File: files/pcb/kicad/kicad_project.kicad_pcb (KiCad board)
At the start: 2 copper layers, 100 x 91.5 mm, 107 parts, among them CON1 USB_MINI_B, IC1 ATMEGA328-A, IC10 MY_FET_P, IC11 DS1307, IC12 MY_NPN, IC13 MY_PNP, IC14 MY_FET_N, IC2 74LC138, IC3 TLP627, IC4 TLP627, IC5 SN74141_K155NA, IC6 TLP627-4, IC7 TLP627-4, IC8 MY_3_TERMINAL_REGULATOR, IC9 ICM7555CD, K1 CONN_3, K2 CONN_3, K3 CONN_3, K4 CONN_3, P1 CONN_6, SW3 SW_PUSH, SW4 SW_PUSH, SW5 SW_PUSH, T1 2SC, U1 NEON, U10 NIXIE_IN_16, U11 DC_JACK, U15 MY_PIN52, U16 MY_PIN52, U17 MY_PIN52, U18 MY_PIN52, U2 NEON, U3 NEON, U4 NEON, U5 NIXIE_IN_16, U6 NIXIE_IN_16, U7 NIXIE_IN_16, U8 NIXIE_IN_16, U9 NIXIE_IN_16, X1 12MHz, X2 32.768kHz

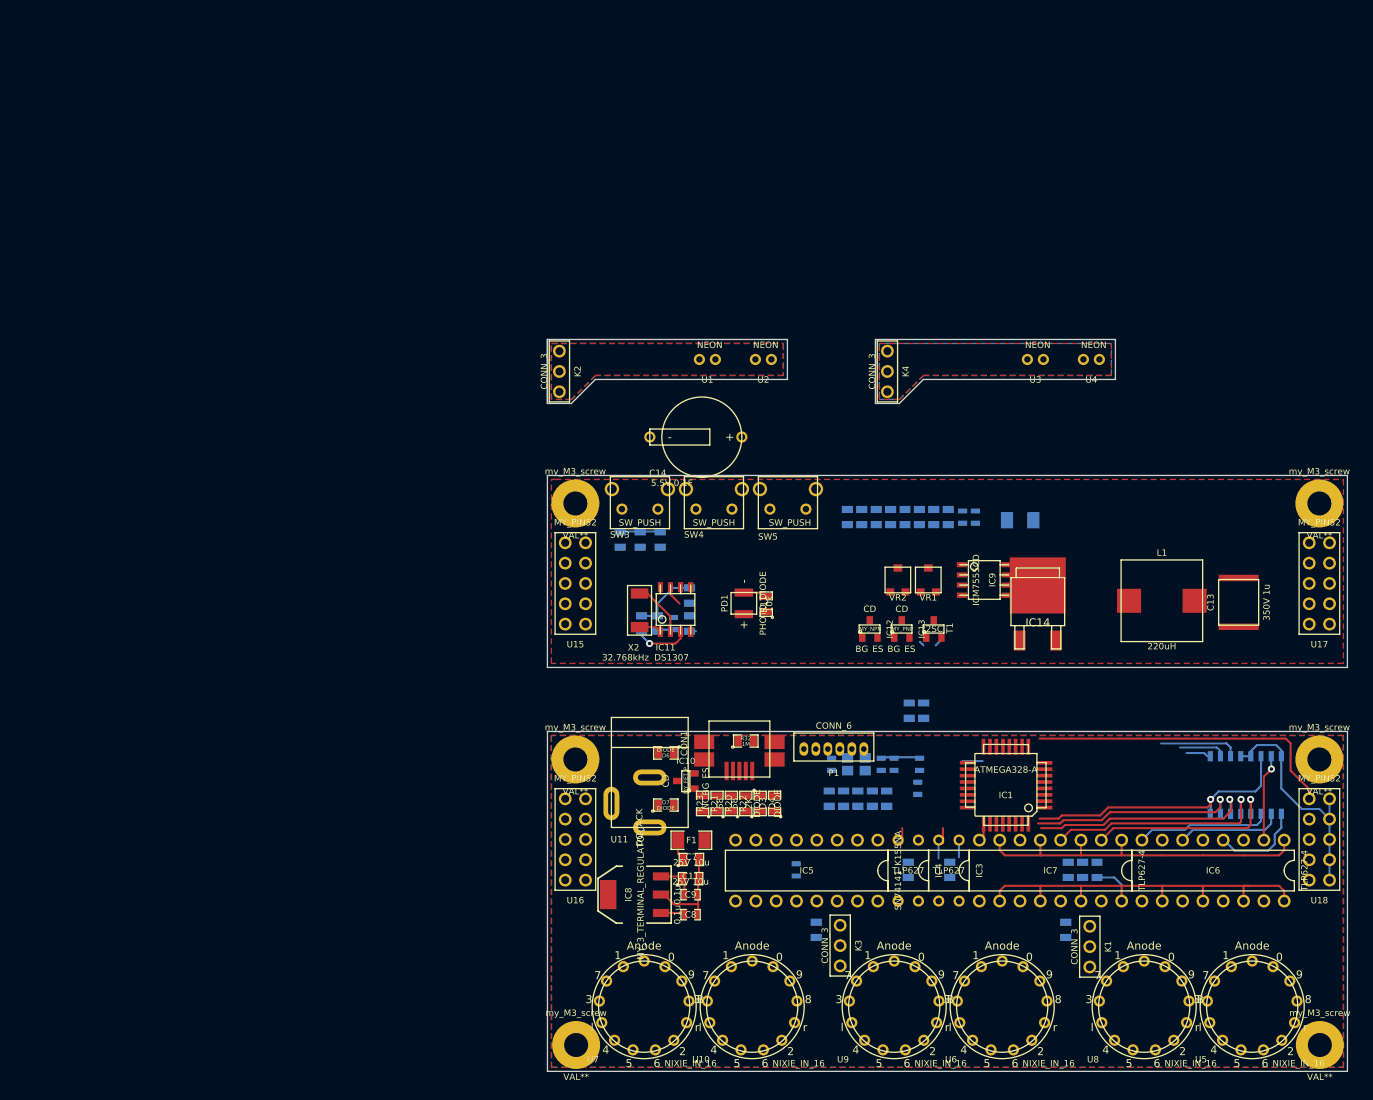
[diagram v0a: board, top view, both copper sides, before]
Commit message: PCB更新
ニキシー管の足を接続
電源仮接続
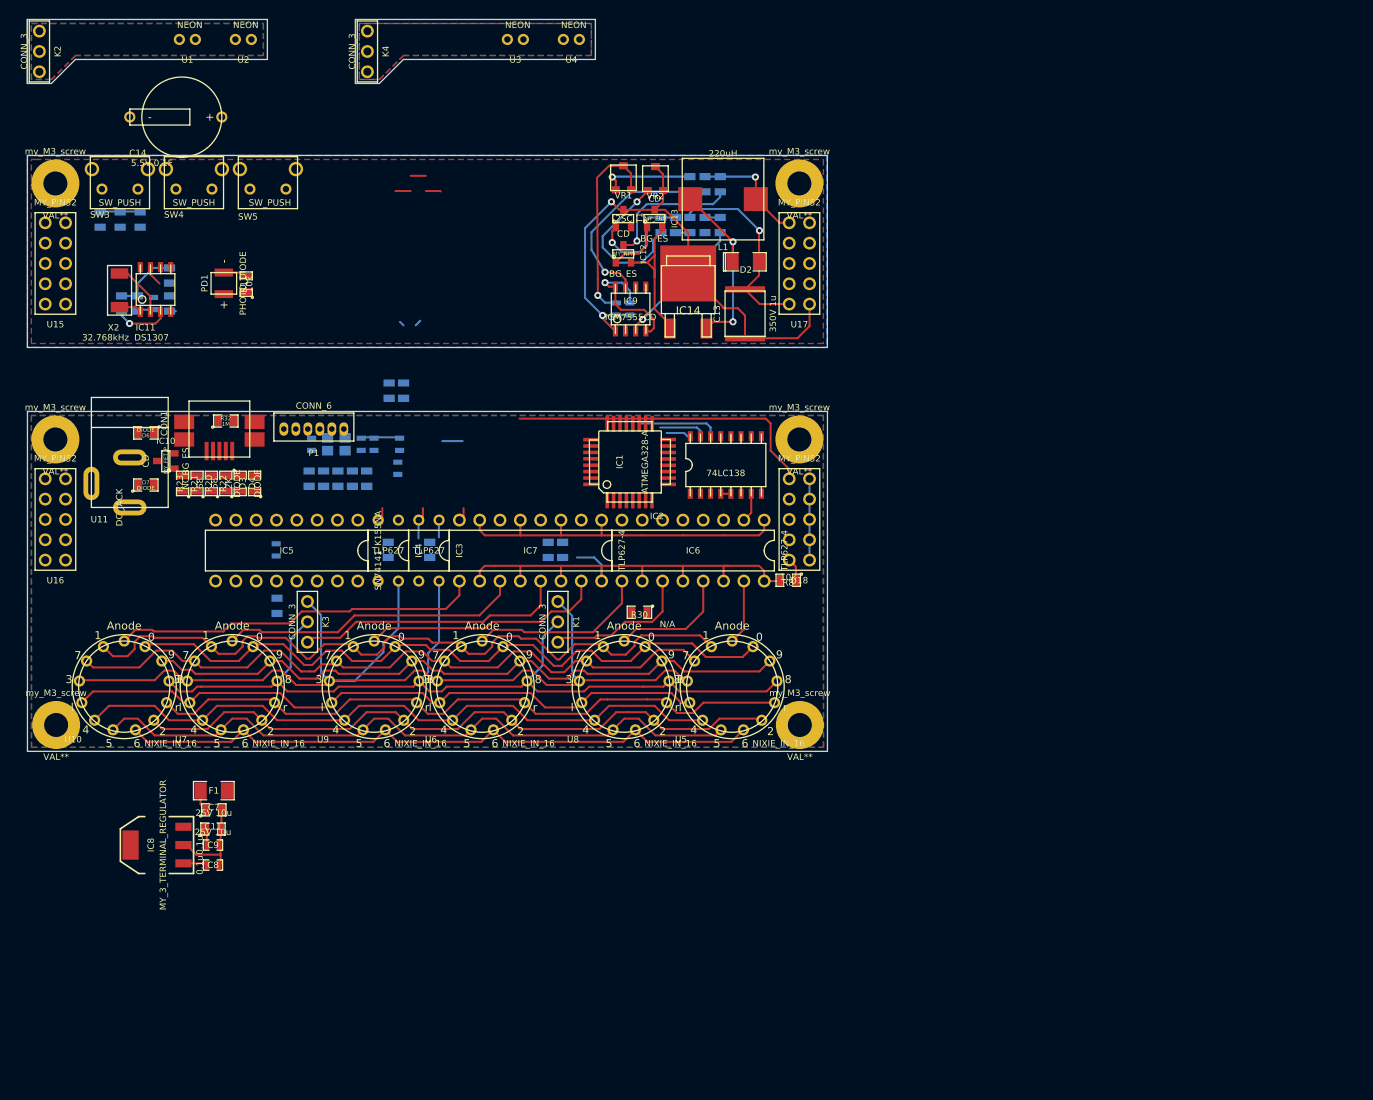
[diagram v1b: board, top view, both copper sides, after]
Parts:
- D2, IC2, R30, R8: moved to F.Cu
- moved U10 88.1 mm to (107.8, 132.7)
- moved R31 78.6 mm to (126.9, 122.6), turned to 90 degrees
- moved K3 77.9 mm to (130.7, 124.6)
- moved K1 77.9 mm to (162.0, 124.6)
- moved U17 76.3 mm to (192.2, 79.8)
- moved U18 76.3 mm to (192.2, 111.8)
- moved my_M3_screw 76.3 mm to (192.2, 69.8)
- moved my_M3_screw 76.3 mm to (192.2, 101.8)
- moved C14 76.3 mm to (115.0, 61.5)
- moved C18 76.3 mm to (111.5, 84.8)
- moved C3 76.3 mm to (142.7, 95.7)
- moved C6 76.3 mm to (142.0, 105.4)
- moved CON1 76.3 mm to (119.7, 99.8)
- moved D1 76.3 mm to (140.9, 95.7)
- moved D4 76.3 mm to (124.1, 107.3)
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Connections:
- C9 pad 1: +5V -> N-0000094
- D6 pad 2: +9V -> +5V
- D7 pad 1: N-0000095 (its old number) -> N-0000094
- D7 pad 2: +9V -> +5V
- IC10 pad 1: N-0000095 (its old number) -> N-0000094
- IC8 pad 3: +5V -> N-0000094
- U11 pad 1: N-0000095 (its old number) -> +9V
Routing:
- net /nixie/Sheet53F9F7BA/dot_cathode_r: track 0.00 -> 122.3 mm
- net /nixie/Sheet53F9F7BA/dot_cathode_l: track 0.00 -> 112.9 mm
- net /nixie/N5: track 0.00 -> 90.6 mm
- net /nixie/N4: track 0.00 -> 87.3 mm
- net /nixie/N6: track 0.00 -> 86.8 mm
- net /nixie/N9: track 0.00 -> 84.7 mm
- net /nixie/N3: track 0.00 -> 84.1 mm
- net /nixie/N1: track 0.00 -> 84.0 mm
- net /nixie/N8: track 0.00 -> 83.5 mm
- net /nixie/N2: track 0.00 -> 83.0 mm
- net /nixie/N0: track 0.00 -> 82.2 mm
- net /nixie/N7: track 0.00 -> 82.1 mm
- net PINGND: track 2.08 -> 71.0 mm, vias 0 -> 2
- net /nixie/Sheet53F9F7BA/6: track 0.00 -> 46.2 mm
- net +5V: track 40.2 -> 2.08 mm, vias 1 -> 0
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- added copper zone on B.Cu, net PINGND
- added copper zone on F.Cu, net PINGND

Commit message: PCB更新
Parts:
- added R33: R, SM0805, F.Cu at (167.1, 68.3)
- C10, C12, C18, D5, R12, R13, R14, R15, R16, R17, R18, R19, R27, R28, R29: moved to F.Cu
- C11, C7, C8, C9, D3, D4, D6, D7, F1, R20, R21, R22, R23, R32: moved to B.Cu
- moved C8 54.0 mm to (117.4, 101.0), turned to 90 degrees
- moved C9 51.6 mm to (115.3, 101.0), turned to 90 degrees
- moved C11 49.8 mm to (110.9, 101.3), turned to 270 degrees
- moved IC8 48.4 mm to (117.5, 104.4), turned to 180 degrees
- moved C7 47.4 mm to (119.8, 100.7), turned to 90 degrees
- moved P1 40.9 mm to (172.4, 100.2)
- moved F1 39.8 mm to (117.0, 106.0), turned to 0 degrees
- moved X2 33.2 mm to (140.4, 81.4), turned to 180 degrees
- moved C1 31.5 mm to (170.5, 104.1)
- moved C4 31.3 mm to (168.6, 104.1)
- moved C5 31.3 mm to (162.4, 104.1)
- moved X1 31.3 mm to (166.6, 104.9)
- moved R29 29.9 mm to (143.4, 84.0)
- moved C14 27.0 mm to (139.6, 72.6)
- moved IC11 26.6 mm to (138.2, 85.8), turned to 270 degrees
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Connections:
- IC13 pad 3: PINGND -> N-0000098
- U15 pad 10: PIN5V -> PINADC6
- U15 pad 4: (no net) -> PIN9V
- U15 pad 6: PINSCL -> PIN5V
- U15 pad 7: PINSDA -> PINSCL
- U15 pad 8: PINCLKOUT -> PINSDA
- U15 pad 9: PINADC6 -> PINCLKOUT
- U16 pad 10: +5V -> /ADC6
- U16 pad 4: (no net) -> +9V
- U16 pad 6: /SCL -> +5V
- U16 pad 7: /SDA -> /SCL
- U16 pad 8: /PD4 -> /SDA
- U16 pad 9: /ADC6 -> /PD4
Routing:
- net PINGND: track 71.0 -> 209.4 mm
- net PIN9V: track 31.1 -> 145.0 mm, vias 2 -> 3
- net GND: track 28.4 -> 141.5 mm, vias 0 -> 7
- net +5V: track 2.08 -> 45.3 mm, vias 0 -> 5
- net PIN5V: track 5.05 -> 47.3 mm, vias 0 -> 1
- net PINADC6: track 3.01 -> 44.3 mm, vias 0 -> 1
- net N-0000089: track 0.00 -> 36.6 mm, vias 0 -> 3
- net /nixie/L8: track 1.91 -> 35.5 mm, vias 0 -> 1
- net /nixie/L7: track 0.00 -> 31.5 mm, vias 0 -> 1
- net +9V: track 39.5 -> 8.96 mm
- net N-0000090: track 0.00 -> 29.6 mm, vias 0 -> 2
- net N-00000107: track 0.00 -> 29.5 mm
- net N-00000110: track 0.00 -> 29.3 mm
- net (no net): track 28.7 -> 0.00 mm
- net /nixie/L6: track 0.00 -> 27.8 mm, vias 0 -> 1
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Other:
- board text added: "Caution 170V"

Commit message: 基板が描けた
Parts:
- added U12: MY_PIN72, my_pin72, F.Cu at (147.7, 69.8)
- added U13: MY_PIN72, my_pin72, F.Cu at (147.4, 101.8)
- C1, C2, C3, C4, C5, C6, D1, R1, R2, R3, X1: moved to F.Cu
- C10, R30: moved to B.Cu
- moved C4 40.7 mm to (131.2, 88.2), turned to 270 degrees
- moved X1 40.6 mm to (131.0, 85.4), turned to 90 degrees
- moved R4 37.7 mm to (134.6, 70.3)
- moved R5 36.9 mm to (136.5, 70.3)
- moved C5 36.8 mm to (129.2, 88.2), turned to 270 degrees
- moved PD1 34.6 mm to (153.9, 74.5), turned to 0 degrees
- moved C1 34.2 mm to (147.1, 79.1)
- moved C2 33.9 mm to (131.0, 79.8)
- moved C14 33.1 mm to (108.2, 83.0), turned to 90 degrees
- moved IC1 31.3 mm to (138.4, 79.8), turned to 0 degrees
- moved D1 29.7 mm to (153.9, 80.5), turned to 0 degrees
- moved R11 28.7 mm to (150.6, 74.6)
- moved R3 28.2 mm to (153.9, 78.7), turned to 180 degrees
- moved P1 25.3 mm to (150.7, 87.2), turned to 180 degrees
- moved R1 25.3 mm to (149.0, 81.5), turned to 90 degrees
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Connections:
- net N-00000106 renamed /nixie/Sheet53F9F7BA/NEL2
- net N-00000107 renamed /nixie/Sheet53F9F7BA/NEG2
- net N-00000108 renamed /nixie/Sheet53F9F7BA/NEU2
- net N-00000109 renamed /nixie/Sheet53F9F7BA/NEL1
- net N-00000110 renamed /nixie/Sheet53F9F7BA/NEG1
- net N-00000111 renamed /nixie/Sheet53F9F7BA/NEU1
- C1 pad 2: GND -> PINGND
- C2 pad 1: +5V -> PIN5V
- C2 pad 2: GND -> PINGND
- C3 pad 2: GND -> PINGND
- C4 pad 2: GND -> PINGND
- C5 pad 2: GND -> PINGND
- D1 pad 2: +5V -> PIN5V
- IC1 pad 1: /Sheet53F8CD20/D- -> /INT1_D-
- IC1 pad 10: /PD6 -> /Sheet53F8FD69/B
- IC1 pad 11: /PD7 -> /Sheet53F8FD69/A
- IC1 pad 18: +5V -> PIN5V
- IC1 pad 19: /ADC6 -> /Sheet53F8BA4D/out
- IC1 pad 2: /PD4 -> /Sheet53F905A8/CLKOUT
- IC1 pad 21: GND -> PINGND
- IC1 pad 27: /SDA -> /Sheet53F905A8/SDA
- IC1 pad 28: /SCL -> /Sheet53F905A8/SCL
- IC1 pad 3: GND -> PINGND
- IC1 pad 32: /Sheet53F8CD20/D+ -> /INT0_D+
- IC1 pad 4: +5V -> PIN5V
- IC1 pad 5: GND -> PINGND
- IC1 pad 6: +5V -> PIN5V
- IC1 pad 9: /PD5 -> /Sheet53F8FD69/Push
- IC11 pad 5: PINSDA -> /Sheet53F905A8/SDA
- IC11 pad 6: PINSCL -> /Sheet53F905A8/SCL
- IC11 pad 7: PINCLKOUT -> /Sheet53F905A8/CLKOUT
- IC2 pad 1: /PB0 -> /PINPB0
- IC2 pad 2: /PB1 -> /PINPB1
- IC2 pad 3: /PB2 -> /PINPB2
- IC3 pad 2: /MOSI -> /PINPB3
- IC4 pad 2: /MISO -> /PINPB4
- IC5 pad 11: /nixie/N6 -> /nixie/N8
- IC5 pad 13: /nixie/N5 -> /nixie/N4
- IC5 pad 14: /nixie/N4 -> /nixie/N5
- IC5 pad 15: /nixie/N3 -> /nixie/N2
- IC5 pad 16: /nixie/N2 -> /nixie/N3
- IC5 pad 3: /PC3 -> /PINPC3
- IC5 pad 4: /PC2 -> /PINPC2
- IC5 pad 6: /PC1 -> GND
- IC5 pad 7: /PC0 -> GND
- IC5 pad 9: /nixie/N8 -> /nixie/N6
- P1 pad 1: /RESET -> PINGND
- P1 pad 2: /SCK -> /RESET
- P1 pad 3: GND -> PIN5V
- P1 pad 4: /MISO -> /SCK
- P1 pad 5: /MOSI -> /MISO
- P1 pad 6: +5V -> /MOSI
- PD1 pad 2: PINADC6 -> /Sheet53F8BA4D/out
- R1 pad 1: +5V -> PIN5V
- R11 pad 2: PINADC6 -> /Sheet53F8BA4D/out
- R20 pad 1: /Sheet53F8CD20/D- -> PIND-
- R21 pad 1: /Sheet53F8CD20/D+ -> PIND+
- R24 pad 2: PINPD5 -> /Sheet53F8FD69/A
- R25 pad 2: PINPD6 -> /Sheet53F8FD69/B
- R26 pad 2: PINPD7 -> /Sheet53F8FD69/Push
- R29 pad 2: PINCLKOUT -> /Sheet53F905A8/CLKOUT
- R3 pad 1: +5V -> PIN5V
- R4 pad 1: +5V -> PIN5V
- R4 pad 2: /SCL -> /Sheet53F905A8/SCL
- R5 pad 1: +5V -> PIN5V
- R5 pad 2: /SDA -> /Sheet53F905A8/SDA
- SW3 pad 1: PINPD5 -> /Sheet53F8FD69/A
- SW4 pad 1: PINPD6 -> /Sheet53F8FD69/B
- SW5 pad 1: PINPD7 -> /Sheet53F8FD69/Push
- U15 pad 1: PINPD5 -> PIN5V
- U15 pad 10: PINADC6 -> PINGND
- U15 pad 2: PINPD6 -> PINGND
- U15 pad 3: PINPD7 -> PINGND
- U15 pad 6: PIN5V -> PINGND
- U15 pad 7: PINSCL -> PINGND
- U15 pad 8: PINSDA -> PINGND
- U15 pad 9: PINCLKOUT -> PINGND
- U16 pad 1: /PD5 -> +5V
- U16 pad 10: /ADC6 -> GND
- U16 pad 2: /PD6 -> GND
- U16 pad 3: /PD7 -> GND
- U16 pad 6: +5V -> GND
- U16 pad 7: /SCL -> GND
- U16 pad 8: /SDA -> GND
- U16 pad 9: /PD4 -> GND
- U17 pad 1: PIN9V -> PINGND
- U17 pad 10: (no net) -> PINGND
- U17 pad 2: (no net) -> PINGND
- U17 pad 3: (no net) -> PINGND
- U17 pad 4: (no net) -> PINGND
- U17 pad 7: (no net) -> PINGND
- U17 pad 8: (no net) -> PINGND
- U17 pad 9: (no net) -> PINGND
- U18 pad 1: +9V -> GND
- U18 pad 2: (no net) -> GND
- U18 pad 3: (no net) -> GND
- U18 pad 4: (no net) -> GND
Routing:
- net GND: track 141.5 -> 296.2 mm, vias 7 -> 5
- net PINGND: track 209.4 -> 323.2 mm, vias 2 -> 8
- net +5V: track 45.3 -> 158.5 mm
- net PIN5V: track 47.3 -> 126.1 mm, vias 1 -> 4
- net /RESET: track 0.00 -> 58.9 mm, vias 0 -> 1
- net /Sheet53F8FD69/A: track 0.00 -> 45.2 mm, vias 0 -> 1
- net /nixie/N1: track 84.0 -> 129.1 mm, vias 0 -> 1
- net /nixie/N0: track 82.2 -> 127.0 mm, vias 0 -> 1
- net PINADC6: track 44.3 -> 0.00 mm, vias 1 -> 0
- net /Sheet53F8FD69/B: track 0.00 -> 38.0 mm, vias 0 -> 1
- net /Sheet53F8FD69/Push: track 0.00 -> 33.2 mm, vias 0 -> 1
- net /PINPB2: track 0.00 -> 32.6 mm
- net /nixie/N9: track 84.7 -> 116.2 mm
- net /Sheet53F905A8/SDA: track 0.00 -> 30.3 mm, vias 0 -> 2
- net /Sheet53F905A8/SCL: track 0.00 -> 29.0 mm, vias 0 -> 2
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- added copper zone on B.Cu, net /nixie/Sheet53F9F7BA/NEG1
- added copper zone on F.Cu, net /nixie/Sheet53F9F7BA/NEG1
- added copper zone on B.Cu, net /nixie/Sheet53F9F7BA/NEG2
- added copper zone on F.Cu, net /nixie/Sheet53F9F7BA/NEG2
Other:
- board size 100 x 91.5 mm -> 100.2 x 91.8 mm
- board text added: "CAUTION 170V!"
- board text removed: "Caution 170V"

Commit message: DRC完了
あとはシルク移動かなぁ
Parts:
- K4, U3, U4: moved to B.Cu
- moved U4 36.1 mm to (129.7, 64.3), turned to 180 degrees
- moved U3 24.4 mm to (136.2, 64.3), turned to 180 degrees
- moved K4 21.4 mm to (155.2, 65.8)
- moved K2 12.8 mm to (97.2, 65.8)
- moved U1 12.8 mm to (116.2, 64.3)
- moved U2 12.8 mm to (122.7, 64.3)
- moved IC2 10.4 mm to (172.6, 104.0), turned to 180 degrees
- moved C6 6.03 mm to (179.2, 107.5), turned to 180 degrees
- moved C1 5.80 mm to (147.1, 84.9)
- moved D5 5.80 mm to (116.1, 89.4)
- moved IC1 5.80 mm to (138.4, 85.7)
- moved IC13 5.80 mm to (166.7, 77.6)
- moved IC9 5.80 mm to (165.7, 86.1)
- moved R11 5.80 mm to (150.6, 80.4)
- moved R18 5.80 mm to (182.0, 88.9)
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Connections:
- IC2 pad 10: /nixie/L3 -> /nixie/L6
- IC2 pad 11: /nixie/L4 -> /nixie/L5
- IC2 pad 12: /nixie/L5 -> /nixie/L4
- IC2 pad 13: /nixie/L6 -> /nixie/L3
- IC2 pad 14: /nixie/L7 -> /nixie/L2
- IC2 pad 15: /nixie/L8 -> /nixie/L1
- IC2 pad 7: /nixie/L1 -> /nixie/L8
- IC2 pad 9: /nixie/L2 -> /nixie/L7
- IC5 pad 6: GND -> /PINPC1
- IC5 pad 7: GND -> /PINPC0
- U13 pad 12: GND -> /PINPC0
- U13 pad 3: GND -> /PINPC1
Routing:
- net GND: track 296.2 -> 431.8 mm, vias 5 -> 17
- net PINGND: track 323.2 -> 357.9 mm
- net /PINPC0: track 0.00 -> 30.6 mm
- net /PINPC1: track 0.00 -> 25.9 mm
- net /nixie/L7: track 31.5 -> 15.8 mm, vias 1 -> 0
- net /nixie/L4: track 20.3 -> 5.10 mm, vias 1 -> 0
- net /nixie/L6: track 27.8 -> 12.8 mm, vias 1 -> 0
- net /nixie/L5: track 24.1 -> 9.08 mm, vias 1 -> 0
- net PIN9V: track 152.4 -> 139.2 mm
- net /nixie/L3: track 16.5 -> 5.06 mm, vias 1 -> 0
- net +5V: track 158.5 -> 147.1 mm
- net PIN5V: track 126.1 -> 136.2 mm
- net /nixie/L8: track 35.5 -> 25.4 mm
- net /nixie/L1: track 3.67 -> 12.7 mm
- net /PINPB2: track 32.6 -> 25.6 mm
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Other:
- board size 100.2 x 91.8 mm -> 100 x 79 mm
